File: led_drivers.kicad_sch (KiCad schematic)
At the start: 22 parts, among them IC1 SamacSys_Parts_HT16K33-28SOP, IC2 SamacSys_Parts_HT16K33-28SOP, SW1 SW_Omron_B3FS, SW2 SW_Omron_B3FS, SW3 SW_Omron_B3FS, SW4 SW_Omron_B3FS

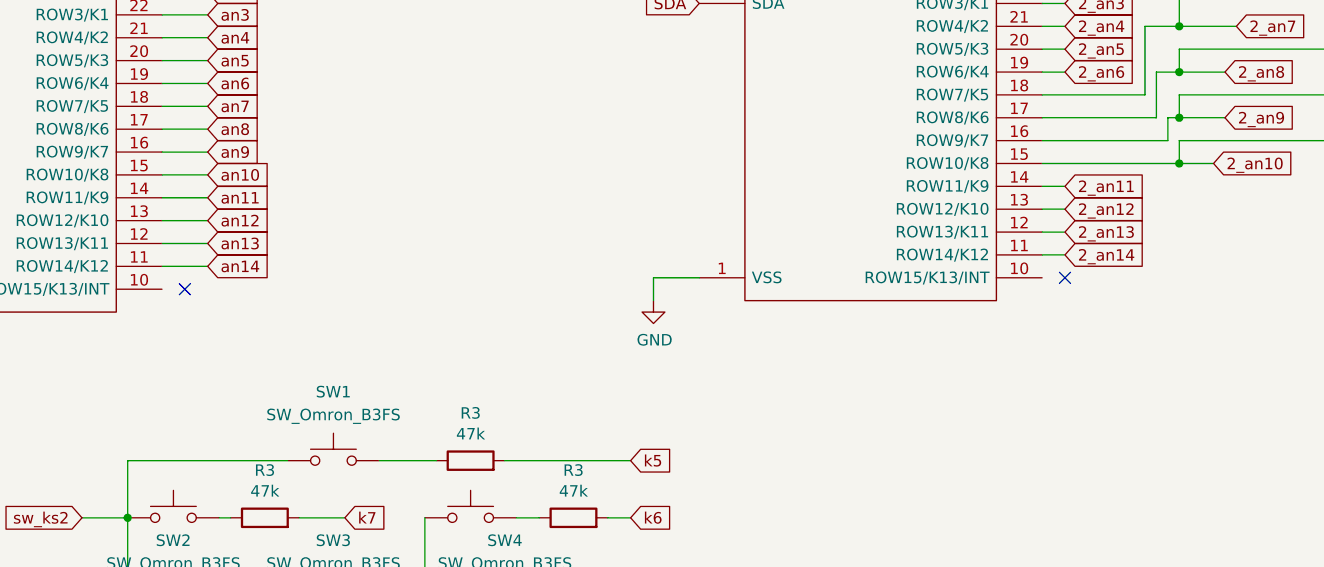
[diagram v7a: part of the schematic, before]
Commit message: Connect decimal points ds3 ds5, add cap
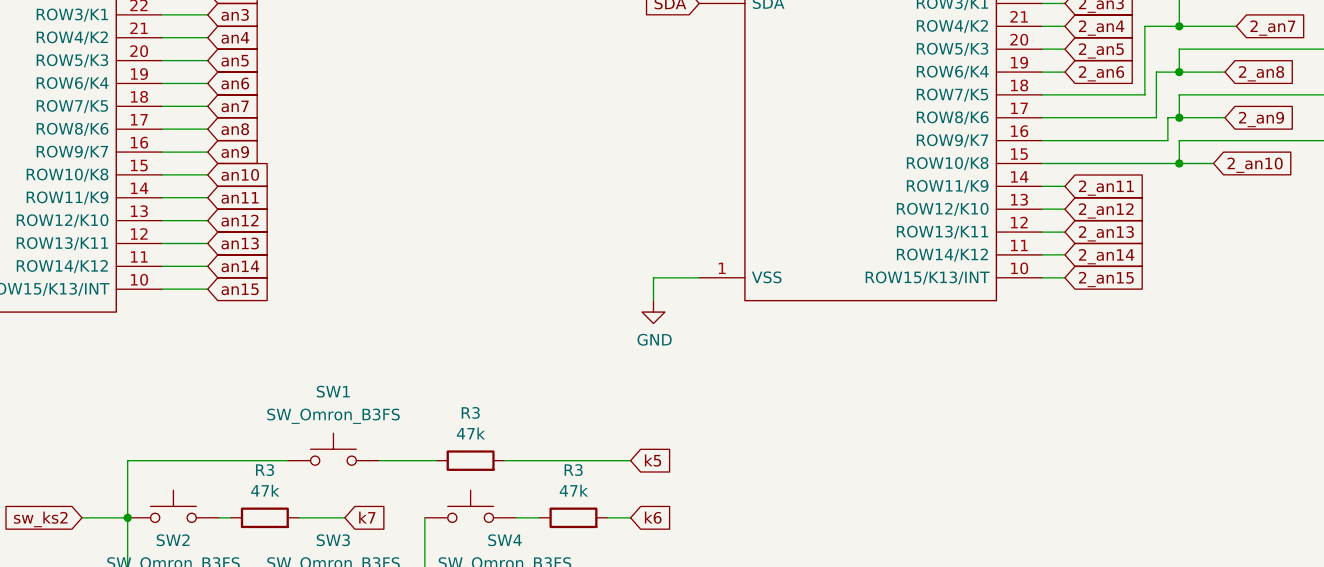
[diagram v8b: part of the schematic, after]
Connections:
- net an15: now reaches IC1.10 (ROW15/K13/INT)
- net 2_an15: now reaches IC2.10 (ROW15/K13/INT)
- no-connect marks 4 -> 2
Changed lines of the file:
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@@
   )
   (no_connect (at 93.98 71.12))
-  (no_connect (at 95.25 114.3))
   (no_connect (at 193.04 69.85))
-  (no_connect (at 193.04 113.03))
   (wire (pts (xy 140.97 49.53) (xy 140.97 52.07))
     (stroke (width 0) (type default))
@@
     (stroke (width 0) (type default))
   )
+  (wire (pts (xy 92.71 114.3) (xy 97.79 114.3))
+    (stroke (width 0) (type default))
+  )
   (wire (pts (xy 88.9 139.7) (xy 83.82 139.7))
     (stroke (width 0) (type default))
   )
   (wire (pts (xy 208.28 54.61) (xy 205.74 54.61))
+    (stroke (width 0) (type default))
+  )
+  (wire (pts (xy 190.5 113.03) (xy 193.04 113.03))
     (stroke (width 0) (type default))
   )
@@
     )
   )
+  (global_label "an15" (shape input) (at 97.79 114.3 0) (fields_autoplaced)
+    (effects (font (size 1.27 1.27)) (justify left))
+    (property "Intersheetrefs" "${INTERSHEET_REFS}" (at 105.4922 114.3 0)
+      (effects (font (size 1.27 1.27)) (justify left) hide)
+    )
+  )
   (global_label "k5" (shape input) (at 222.25 81.28 0)
     (effects (font (size 1.27 1.27)) (justify left))
@@
     )
   )
+  (global_label "2_an15" (shape input) (at 193.04 113.03 0) (fields_autoplaced)
+    (effects (font (size 1.27 1.27)) (justify left))
+    (property "Intersheetrefs" "${INTERSHEET_REFS}" (at 202.9193 113.03 0)
+      (effects (font (size 1.27 1.27)) (justify left) hide)
+    )
+  )
